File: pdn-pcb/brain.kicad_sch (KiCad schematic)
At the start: 5 parts, among them U1 ESP32-S3-WROOM-1(N8R8)

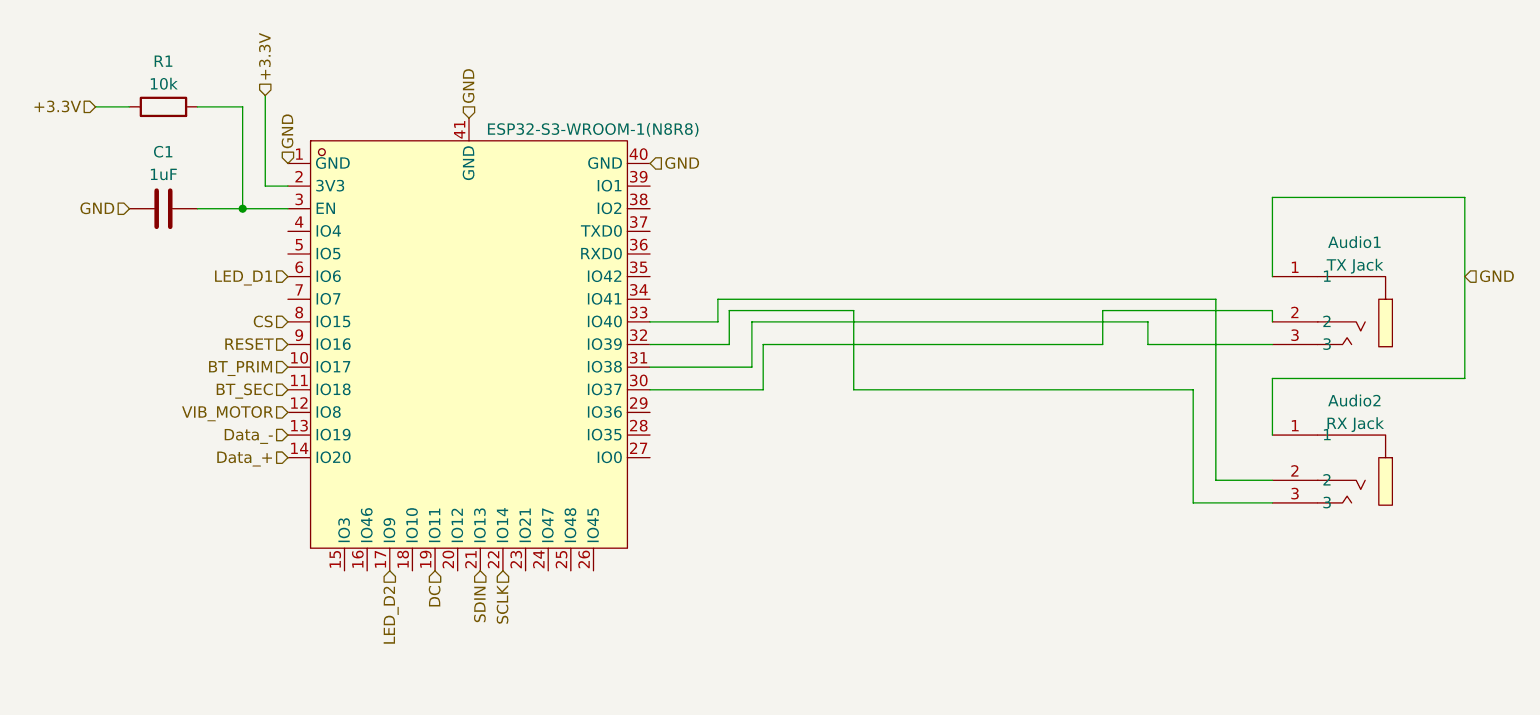
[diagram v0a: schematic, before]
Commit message: Updated 3v3 LDO to an LDL1117, reworked the brain board and added TVS protection.
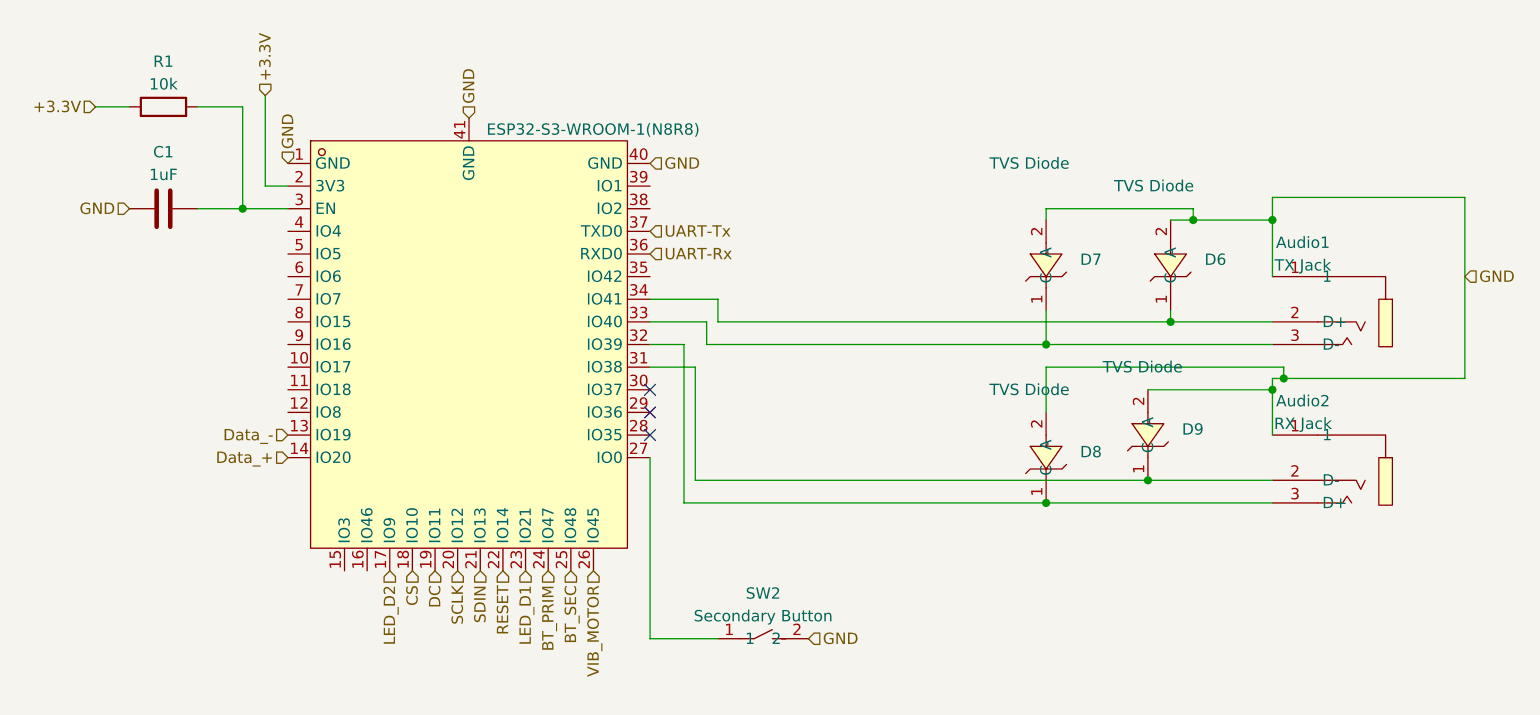
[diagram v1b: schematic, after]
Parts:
- added D6, D7, D8, D9: TVS Diode, global:SOD-323_L1.8-W1.3-LS2.5-RD, symbol global:SD03_C502526
- added SW2: Secondary Button, global:KEY-SMD_L6.0-W3.5-LS8.0, symbol global:TSB013A5026B
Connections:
- net BT_PRIM: now also U1.24 (IO47); no longer U1.10 (IO17)
- net BT_SEC: now also U1.25 (IO48); no longer U1.11 (IO18)
- net CS: now also U1.18 (IO10); no longer U1.8 (IO15)
- net GND: now also D6.2 (A), D7.2 (A), D8.2 (A), D9.2 (A), SW2.2
- net LED_D1: now also U1.23 (IO21); no longer U1.6 (IO6)
- net RESET: now also U1.22 (IO14); no longer U1.9 (IO16)
- net SCLK: now also U1.20 (IO12); no longer U1.22 (IO14)
- net VIB_MOTOR: now also U1.26 (IO45); no longer U1.12 (IO8)
- net at Audio1.2 (D+): now also U1.34 (IO41), D6.1 (C); no longer U1.30 (IO37)
- net at Audio1.3 (D-): now also U1.33 (IO40), D7.1 (C); no longer U1.31 (IO38)
- net at Audio2.2 (D-): now also U1.31 (IO38), D9.1 (C); no longer U1.33 (IO40)
- net at Audio2.3 (D+), U1.32 (IO39): now also D8.1 (C)
- net at U1.27 (IO0): now also SW2.1
- net UART-Rx: now reaches U1.36 (RXD0)
- net UART-Tx: now reaches U1.37 (TXD0)
- no-connect marks 0 -> 3

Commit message: Updated display, user board and display board.
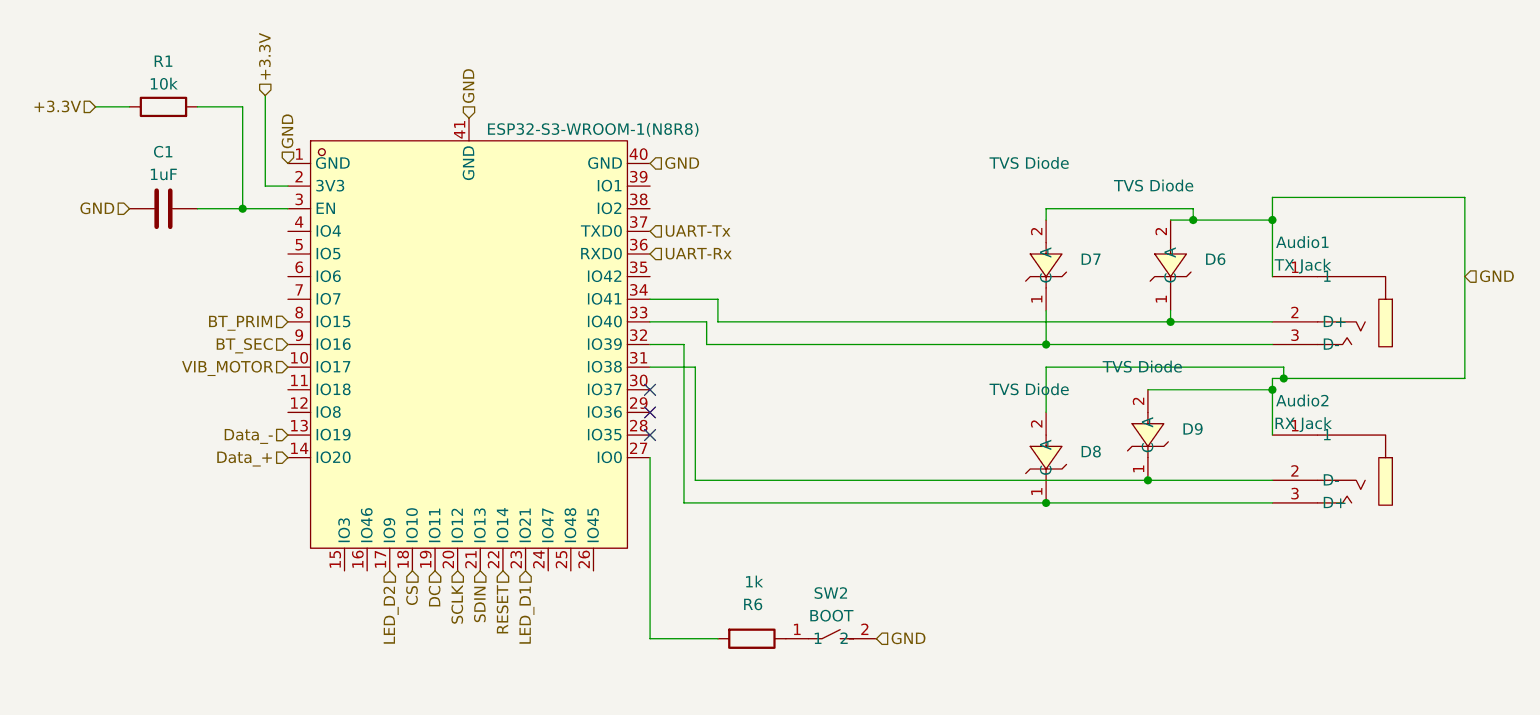
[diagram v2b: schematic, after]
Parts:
- added R6: 1k, Resistor_SMD:R_0603_1608Metric, symbol Device:R
- SW2: value Secondary Button -> BOOT
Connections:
- net BT_PRIM: now also U1.8 (IO15); no longer U1.24 (IO47)
- net BT_SEC: now also U1.9 (IO16); no longer U1.25 (IO48)
- net VIB_MOTOR: now also U1.10 (IO17); no longer U1.26 (IO45)
- net at SW2.1: now also R6.1; no longer U1.27 (IO0)
- new net: R6.2, U1.27 (IO0)
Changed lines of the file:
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@@
     (effects (font (size 1.27 1.27)) (justify right))
   )
-  (hierarchical_label "GND" (shape input) (at 107.95 91.44 0) (fields_autoplaced)
-    (effects (font (size 1.27 1.27)) (justify left))
+  (hierarchical_label "GND" (shape input) (at 115.57 91.44 0) (fields_autoplaced)
+    (effects (font (size 1.27 1.27)) (justify left))
+  )
+  (hierarchical_label "BT_PRIM" (shape input) (at 49.53 55.88 180) (fields_autoplaced)
+    (effects (font (size 1.27 1.27)) (justify right))
+    (property "Intersheetrefs" "${INTERSHEET_REFS}" (at 39.5853 55.88 0)
+      (effects (font (size 1.27 1.27)) (justify right) hide)
+    )
   )
   (hierarchical_label "UART-Rx" (shape input) (at 90.17 48.26 0) (fields_autoplaced)
     (effects (font (size 1.27 1.27)) (justify left))
   )
-  (hierarchical_label "BT_SEC" (shape input) (at 81.28 83.82 270) (fields_autoplaced)
-    (effects (font (size 1.27 1.27)) (justify right))
-    (property "Intersheetrefs" "${INTERSHEET_REFS}" (at 81.28 92.797 90)
+  (hierarchical_label "VIB_MOTOR" (shape input) (at 49.53 60.96 180) (fields_autoplaced)
+    (effects (font (size 1.27 1.27)) (justify right))
+    (property "Intersheetrefs" "${INTERSHEET_REFS}" (at 37.1057 60.96 0)
+      (effects (font (size 1.27 1.27)) (justify right) hide)
+    )
+  )
+  (hierarchical_label "BT_SEC" (shape input) (at 49.53 58.42 180) (fields_autoplaced)
+    (effects (font (size 1.27 1.27)) (justify right))
+    (property "Intersheetrefs" "${INTERSHEET_REFS}" (at 40.553 58.42 0)
       (effects (font (size 1.27 1.27)) (justify right) hide)
     )
@@
     )
   )
-  (hierarchical_label "VIB_MOTOR" (shape input) (at 83.82 83.82 270) (fields_autoplaced)
-    (effects (font (size 1.27 1.27)) (justify right))
-    (property "Intersheetrefs" "${INTERSHEET_REFS}" (at 83.82 96.2443 90)
-      (effects (font (size 1.27 1.27)) (justify right) hide)
-    )
-  )
-  (hierarchical_label "BT_PRIM" (shape input) (at 78.74 83.82 270) (fields_autoplaced)
-    (effects (font (size 1.27 1.27)) (justify right))
-    (property "Intersheetrefs" "${INTERSHEET_REFS}" (at 78.74 93.7647 90)
-      (effects (font (size 1.27 1.27)) (justify right) hide)
+  (symbol (lib_id "global:TSB013A5026B") (at 110.49 91.44 0) (unit 1)
+    (in_bom yes) (on_board yes) (dnp no) (fields_autoplaced)
+    (property "Reference" "SW2" (at 110.49 86.36 0)
+      (effects (font (size 1.27 1.27)))
+    )
+    (property "Value" "BOOT" (at 110.49 88.9 0)
+      (effects (font (size 1.27 1.27)))
+    )
+    (property "Footprint" "global:KEY-SMD_L6.0-W3.5-LS8.0" (at 110.49 99.06 0)
+      (effects (font (size 1.27 1.27)) hide)
+    )
+    (property "Datasheet" "" (at 110.49 91.44 0)
+      (effects (font (size 1.27 1.27)) hide)
+    )
+    (property "LCSC Part" "C2888463" (at 110.49 101.6 0)
+      (effects (font (size 1.27 1.27)) hide)
+    )
+    (pin "1")
+    (pin "2")
+    (instances
+      (project "PDN"
+        (path "/df0bc267-025e-4c4e-a09b-51ff87d0c1db"
+          (reference "SW2") (unit 1)
+        )
+        (path "/df0bc267-025e-4c4e-a09b-51ff87d0c1db/176b62b0-12ec-4a4a-9309-4e23e06b21ff"
+          (reference "SW3") (unit 1)
+        )
+        (path "/df0bc267-025e-4c4e-a09b-51ff87d0c1db/5528999e-e72f-4e39-b507-18d3b44f3b41"
+          (reference "SW4") (unit 1)
+        )
+      )
     )
   )
@@
         (path "/df0bc267-025e-4c4e-a09b-51ff87d0c1db/5528999e-e72f-4e39-b507-18d3b44f3b41"
           (reference "D7") (unit 1)
-        )
-      )
-    )
-  )
-  (symbol (lib_id "global:TSB013A5026B") (at 102.87 91.44 0) (unit 1)
-    (in_bom yes) (on_board yes) (dnp no) (fields_autoplaced)
-    (property "Reference" "SW2" (at 102.87 86.36 0)
-      (effects (font (size 1.27 1.27)))
-    )
-    (property "Value" "Secondary Button" (at 102.87 88.9 0)
-      (effects (font (size 1.27 1.27)))
-    )
-    (property "Footprint" "global:KEY-SMD_L6.0-W3.5-LS8.0" (at 102.87 99.06 0)
-      (effects (font (size 1.27 1.27)) hide)
-    )
-    (property "Datasheet" "" (at 102.87 91.44 0)
-      (effects (font (size 1.27 1.27)) hide)
-    )
-    (property "LCSC Part" "C2888463" (at 102.87 101.6 0)
-      (effects (font (size 1.27 1.27)) hide)
-    )
-    (pin "1")
-    (pin "2")
-    (instances
-      (project "PDN"
-        (path "/df0bc267-025e-4c4e-a09b-51ff87d0c1db"
-          (reference "SW2") (unit 1)
-        )
-        (path "/df0bc267-025e-4c4e-a09b-51ff87d0c1db/176b62b0-12ec-4a4a-9309-4e23e06b21ff"
-          (reference "SW3") (unit 1)
-        )
-        (path "/df0bc267-025e-4c4e-a09b-51ff87d0c1db/5528999e-e72f-4e39-b507-18d3b44f3b41"
-          (reference "SW4") (unit 1)
         )
       )
@@
         )
       )
+    )
+  )
+  (symbol (lib_id "Device:R") (at 101.6 91.44 270) (unit 1)
+    (in_bom yes) (on_board yes) (dnp no)
+    (property "Reference" "R6" (at 102.87 87.63 90)
+      (effects (font (size 1.27 1.27)) (justify right))
+    )
+    (property "Value" "1k" (at 102.87 85.09 90)
+      (effects (font (size 1.27 1.27)) (justify right))
+    )
+    (property "Footprint" "Resistor_SMD:R_0603_1608Metric" (at 101.6 89.662 90)
+      (effects (font (size 1.27 1.27)) hide)
+    )
+    (property "Datasheet" "~" (at 101.6 91.44 0)
+      (effects (font (size 1.27 1.27)) hide)
+    )
+    (property "LCSC Part" "C2759381" (at 101.6 91.44 0)
+      (effects (font (size 1.27 1.27)) hide)
+    )
+    (pin "1")
+    (pin "2")
+    (instances
+      (project "PDN"
+        (path "/df0bc267-025e-4c4e-a09b-51ff87d0c1db"
+          (reference "R6") (unit 1)
+        )
+        (path "/df0bc267-025e-4c4e-a09b-51ff87d0c1db/c306c3c8-b7c4-4bd2-bb28-1ed44c071e88"
+          (reference "R6") (unit 1)
+        )
+        (path "/df0bc267-025e-4c4e-a09b-51ff87d0c1db/5528999e-e72f-4e39-b507-18d3b44f3b41"
+          (reference "R15") (unit 1)
+        )
+      )

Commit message: Update Brain Board.
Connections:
- net DC: now also U1.17 (IO9); no longer U1.19 (IO11)
- net LED_D2: now also U1.21 (IO13); no longer U1.17 (IO9)
- net SDIN: now also U1.19 (IO11); no longer U1.21 (IO13)
- net at Audio2.3 (D+), D8.1 (C): now also U1.31 (IO38); no longer U1.32 (IO39)
- net at Audio2.2 (D-), D9.1 (C): now also U1.32 (IO39); no longer U1.31 (IO38)
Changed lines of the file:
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@@
     (stroke (width 0) (type default))
   )
-  (wire (pts (xy 95.25 73.66) (xy 95.25 60.96))
+  (wire (pts (xy 95.25 58.42) (xy 95.25 73.66))
     (stroke (width 0) (type default))
   )
@@
     (stroke (width 0) (type default))
   )
+  (wire (pts (xy 95.25 58.42) (xy 90.17 58.42))
+    (stroke (width 0) (type default))
+  )
   (wire (pts (xy 44.45 31.75) (xy 39.37 31.75))
     (stroke (width 0) (type default))
@@
     (stroke (width 0) (type default))
   )
-  (wire (pts (xy 93.98 58.42) (xy 90.17 58.42))
-    (stroke (width 0) (type default))
-  )
   (wire (pts (xy 46.99 40.64) (xy 49.53 40.64))
     (stroke (width 0) (type default))
@@
     (stroke (width 0) (type default))
   )
-  (wire (pts (xy 95.25 60.96) (xy 90.17 60.96))
-    (stroke (width 0) (type default))
-  )
   (wire (pts (xy 148.59 55.88) (xy 97.79 55.88))
     (stroke (width 0) (type default))
@@
     (stroke (width 0) (type default))
   )
-  (wire (pts (xy 93.98 76.2) (xy 93.98 58.42))
+  (wire (pts (xy 93.98 76.2) (xy 93.98 60.96))
+    (stroke (width 0) (type default))
+  )
+  (wire (pts (xy 90.17 60.96) (xy 93.98 60.96))
     (stroke (width 0) (type default))
   )
@@
     )
   )
+  (hierarchical_label "LED_D2" (shape input) (at 71.12 83.82 270) (fields_autoplaced)
+    (effects (font (size 1.27 1.27)) (justify right))
+    (property "Intersheetrefs" "${INTERSHEET_REFS}" (at 71.12 92.8575 90)
+      (effects (font (size 1.27 1.27)) (justify right) hide)
+    )
+  )
   (hierarchical_label "BT_SEC" (shape input) (at 49.53 58.42 180) (fields_autoplaced)
     (effects (font (size 1.27 1.27)) (justify right))
@@
     )
   )
+  (hierarchical_label "SDIN" (shape input) (at 66.04 83.82 270) (fields_autoplaced)
+    (effects (font (size 1.27 1.27)) (justify right))
+    (property "Intersheetrefs" "${INTERSHEET_REFS}" (at 66.04 91.1406 90)
+      (effects (font (size 1.27 1.27)) (justify right) hide)
+    )
+  )
+  (hierarchical_label "DC" (shape input) (at 60.96 83.82 270) (fields_autoplaced)
+    (effects (font (size 1.27 1.27)) (justify right))
+    (property "Intersheetrefs" "${INTERSHEET_REFS}" (at 60.96 89.2658 90)
+      (effects (font (size 1.27 1.27)) (justify right) hide)
+    )
+  )
   (hierarchical_label "SCLK" (shape input) (at 68.58 83.82 270) (fields_autoplaced)
     (effects (font (size 1.27 1.27)) (justify right))
@@
     (effects (font (size 1.27 1.27)) (justify left))
   )
-  (hierarchical_label "LED_D2" (shape input) (at 60.96 83.82 270) (fields_autoplaced)
-    (effects (font (size 1.27 1.27)) (justify right))
-    (property "Intersheetrefs" "${INTERSHEET_REFS}" (at 60.96 92.8575 90)
-      (effects (font (size 1.27 1.27)) (justify right) hide)
-    )
-  )
   (hierarchical_label "UART-Tx" (shape input) (at 90.17 45.72 0) (fields_autoplaced)
     (effects (font (size 1.27 1.27)) (justify left))
   )
-  (hierarchical_label "SDIN" (shape input) (at 71.12 83.82 270) (fields_autoplaced)
-    (effects (font (size 1.27 1.27)) (justify right))
-    (property "Intersheetrefs" "${INTERSHEET_REFS}" (at 71.12 91.1406 90)
-      (effects (font (size 1.27 1.27)) (justify right) hide)
-    )
-  )
   (hierarchical_label "GND" (shape input) (at 69.85 33.02 90) (fields_autoplaced)
     (effects (font (size 1.27 1.27)) (justify left))
   )
-  (hierarchical_label "DC" (shape input) (at 66.04 83.82 270) (fields_autoplaced)
-    (effects (font (size 1.27 1.27)) (justify right))
-    (property "Intersheetrefs" "${INTERSHEET_REFS}" (at 66.04 89.2658 90)
-      (effects (font (size 1.27 1.27)) (justify right) hide)
-    )
-  )
   (hierarchical_label "Data_+" (shape input) (at 49.53 71.12 180) (fields_autoplaced)
